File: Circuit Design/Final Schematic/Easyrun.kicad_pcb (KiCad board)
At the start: 2 copper layers, 100 x 92.5 mm, 78 parts, among them U1 ESP32-WROOM-32

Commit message: PCB almost ready
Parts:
- moved CByBa1 4.84 mm to (148.4, 103.3), turned to 0 degrees
- moved C_b1 2.75 mm to (94.6, 125.0)
- moved CB3 2.70 mm to (91.2, 109.6), turned to 90 degrees
- moved CBy5 2.32 mm to (126.2, 111.5), turned to 90 degrees
- moved RI2C1 2.09 mm to (155.2, 86.0)
- moved RI2C2 2.09 mm to (158.6, 86.0)
- moved R_Prog1 1.73 mm to (154.4, 93.0)
- moved REF** 1.58 mm to (76.4, 95.7)
- moved QBoo1 1.53 mm to (107.5, 89.9)
- moved R_RED1 1.52 mm to (140.3, 93.2)
- moved UB5v0 1.48 mm to (121.2, 125.1)
- moved D1 1.44 mm to (109.7, 95.7)
- moved D_RED1 1.27 mm to (141.0, 88.3)
- moved FB1 1.14 mm to (167.3, 115.6)
- moved RBtn2 1.12 mm to (112.2, 80.3)
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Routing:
- net +3V3: track 0.00 -> 296.0 mm, vias 0 -> 5
- net +5V: track 0.00 -> 133.2 mm, vias 0 -> 1
- net /PowerModule/Battery Charge/Vo_bat: track 0.00 -> 121.6 mm, vias 0 -> 3
- net /MISO: track 0.00 -> 114.0 mm
- net /PowerModule/Buck5v0: track 0.00 -> 111.6 mm, vias 0 -> 5
- net /I2C2: track 0.00 -> 101.3 mm, vias 0 -> 2
- net /Rst_2: track 0.00 -> 98.5 mm, vias 0 -> 2
- net /I2C1: track 0.00 -> 94.3 mm, vias 0 -> 2
- net /CS_Display: track 0.00 -> 87.6 mm, vias 0 -> 2
- net /Rst_D: track 0.00 -> 85.9 mm, vias 0 -> 2
- net STDBY: track 0.00 -> 75.8 mm, vias 0 -> 2
- net /D/C: track 0.00 -> 71.4 mm, vias 0 -> 1
- net CHRG: track 0.00 -> 66.8 mm
- net Net-(DBoo1-Pad2): track 0.00 -> 66.5 mm
- net /CS_Lector2: track 0.00 -> 60.2 mm, vias 0 -> 1
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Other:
- board size 100 x 92.5 mm -> 100.4 x 94.2 mm

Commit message: Final
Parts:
- moved RBtn2 34.0 mm to (144.7, 90.1)
- moved J_Tap_1 31.9 mm to (192.1, 130.6)
- moved Lb1 31.9 mm to (115.8, 128.2)
- moved B1 31.9 mm to (121.3, 94.2)
- moved B1_1 31.9 mm to (121.3, 89.8)
- moved B2 31.9 mm to (136.1, 94.2)
- moved B2_1 31.9 mm to (136.1, 89.7)
- moved CB4 31.9 mm to (142.8, 94.4)
- moved CBy3 31.9 mm to (148.2, 114.3)
- moved CBy5 31.9 mm to (156.7, 121.1)
- moved CByBa1 31.9 mm to (178.9, 112.8)
- moved C_cv1 31.9 mm to (193.1, 113.5)
- moved Cby2 31.9 mm to (197.4, 112.8)
- moved D1 31.9 mm to (140.2, 105.3)
- moved DB5 31.9 mm to (154.5, 112.7)
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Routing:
- net +5V: track 133.2 -> 270.9 mm
- net /Butt_D: track 19.3 -> 31.8 mm, vias 0 -> 1
- net +3V3: track 296.0 -> 297.5 mm
- net GND: vias 0 -> 181
- added copper zone on B.Cu, net GND
- added copper zone on F.Cu, net GND

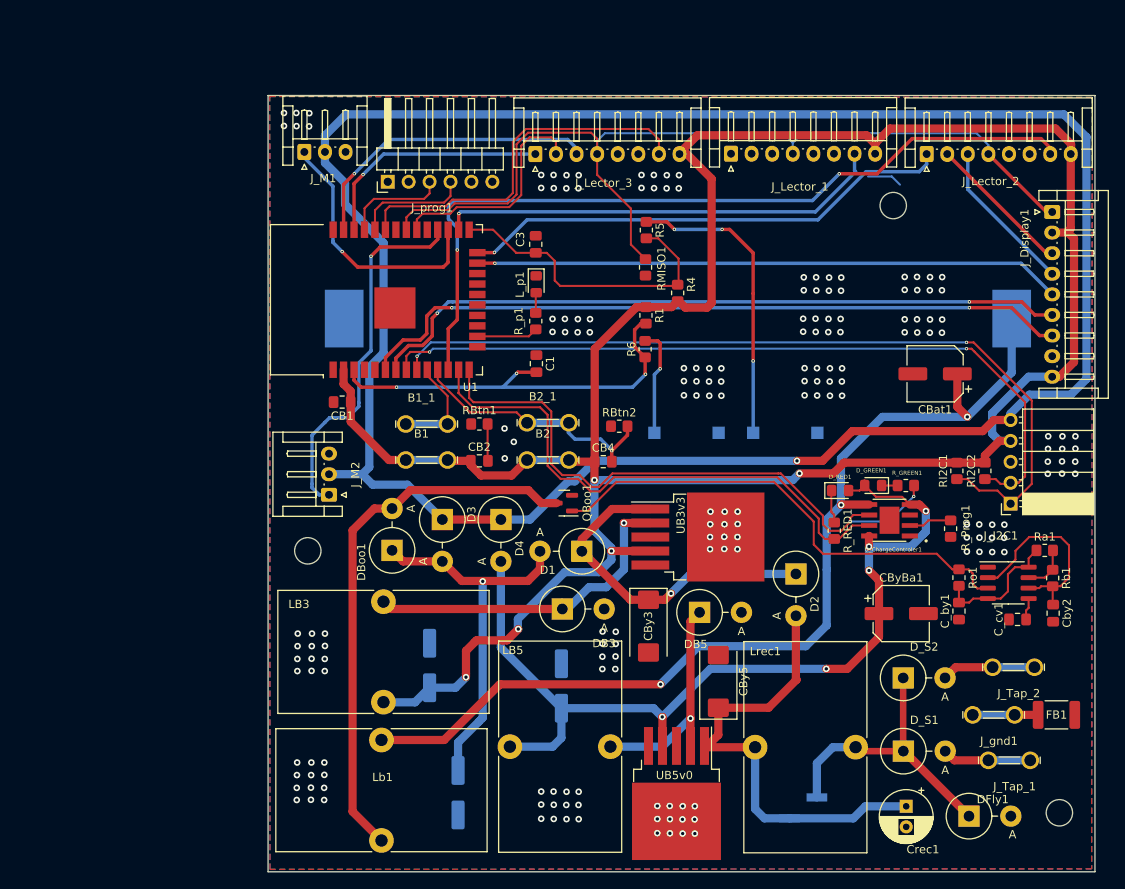
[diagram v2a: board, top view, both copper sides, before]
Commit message: Ruteo de PCB
Se agregó el ruteo de la PCB verificando las conexiones
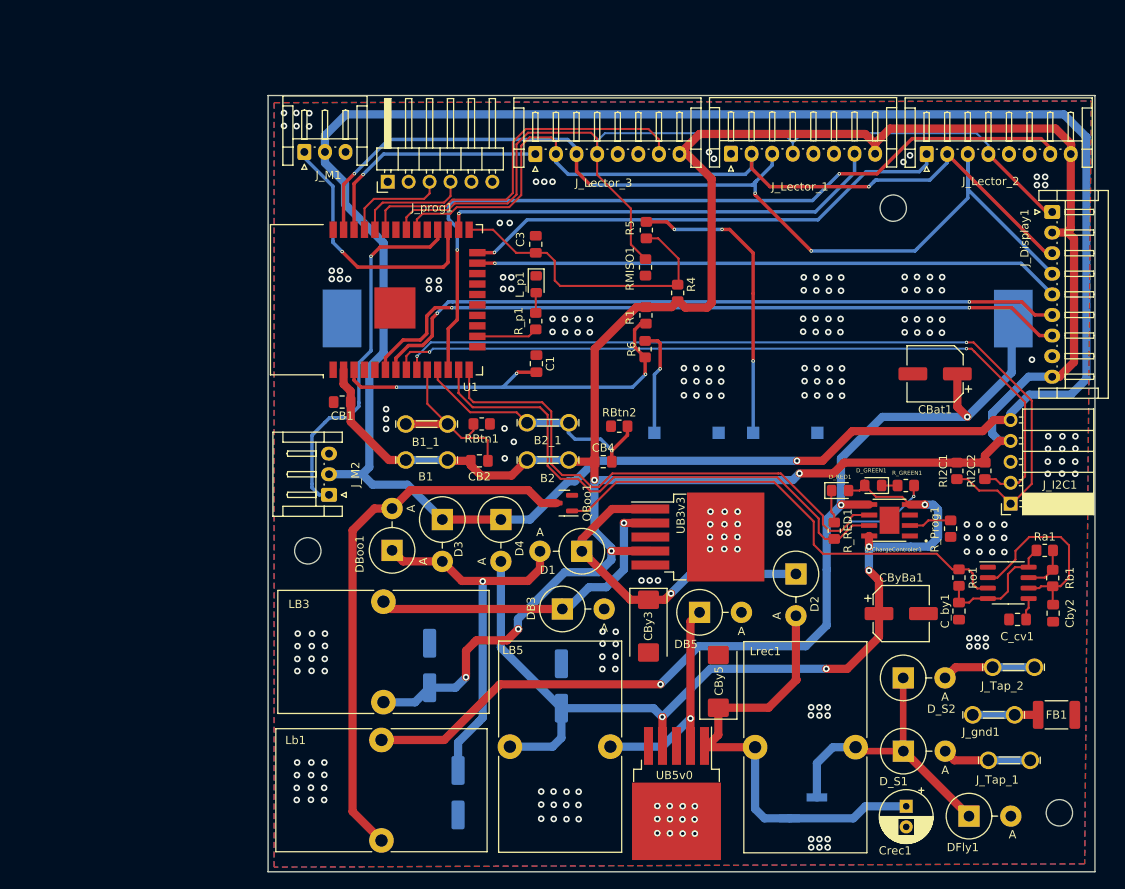
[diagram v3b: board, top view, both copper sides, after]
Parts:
- moved REF** 0.31 mm to (178.0, 63.6)
- moved RBtn1 0.28 mm to (128.0, 89.8), turned to 180 degrees
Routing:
- net /MOSI: track 56.0 -> 123.2 mm, vias 1 -> 4
- net /SCK: track 45.2 -> 101.8 mm, vias 0 -> 1
- net /Butt_No_D: track 17.2 -> 23.0 mm
- net (no net): track 4.28 -> 0.00 mm
- net /PowerModule/Buck5v0: track 111.6 -> 115.1 mm
- net GND: vias 181 -> 220

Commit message: Corrección tamaño de vías
Se corrigió el tamaño de las vías pasantes de la PCB
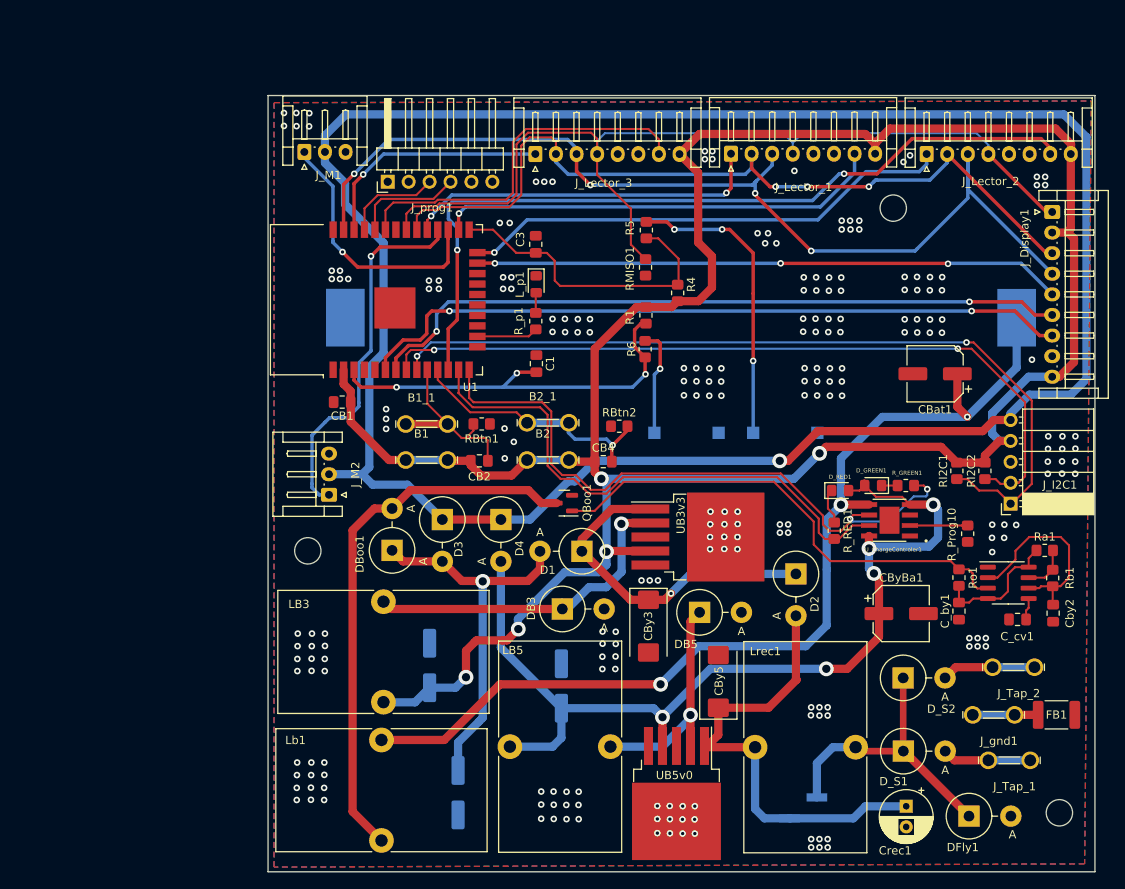
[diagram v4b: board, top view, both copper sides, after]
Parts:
- moved R_Prog10 2.16 mm to (187.0, 103.1)
- moved BT1 0.42 mm to (189.4, 77.2)
- renumbered R_Prog1 to R_Prog10
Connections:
- U1 pad 29: /CS_Lector_1 -> /CS_Lector1
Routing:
- net /CS_Lector1: track 0.00 -> 45.1 mm, vias 0 -> 2
- net STDBY: track 75.8 -> 79.1 mm
- net Net-(R_Prog10-Pad1): track 5.20 -> 6.30 mm
- net /Prog_Rx: track 12.7 -> 11.8 mm
- net +3V3: track 297.6 -> 296.8 mm
- net /Prog_Tx: track 14.0 -> 13.3 mm
- net Net-(DB5-Pad1): track 27.8 -> 28.3 mm
- net /SCK: track 101.8 -> 102.0 mm, vias 1 -> 3
- net /D/C: vias 1 -> 3
- net GND: vias 220 -> 227
